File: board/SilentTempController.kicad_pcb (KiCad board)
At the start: 2 copper layers, 100 x 100 mm, 97 parts, among them J1 Barrel_Jack_Switch, J10 Conn_01x02_Pin, J11 Conn_01x02_Pin, J12 Screw_Terminal_01x02, J13 Screw_Terminal_01x02, J14 Screw_Terminal_01x02, J15 Screw_Terminal_01x02, J2 Screw_Terminal_01x02, J3 Conn_01x02_Pin, J4 Screw_Terminal_01x02, J5 Conn_01x02_Pin, J6 Screw_Terminal_01x02, J7 Conn_01x02_Pin, J8 Screw_Terminal_01x02, J9 Conn_01x02_Pin, Q1 2N3904, Q10 2N3904, Q11 2N3906, Q12 IRLZ44N, Q13 2N3904, Q14 2N3904, Q15 2N3906, Q16 IRLZ44N, Q17 2N3904, Q2 2N3906, Q3 IRLZ44N, Q4 2N3904, Q5 2N3904, Q6 2N3904, Q7 2N3906, Q8 IRLZ44N, Q9 2N3904, SW1 SW_Push, SW2 SW_Push, SW3 SW_Push, SW4 SW_Push, SW5 SW_Push, U1 LM7805_TO220

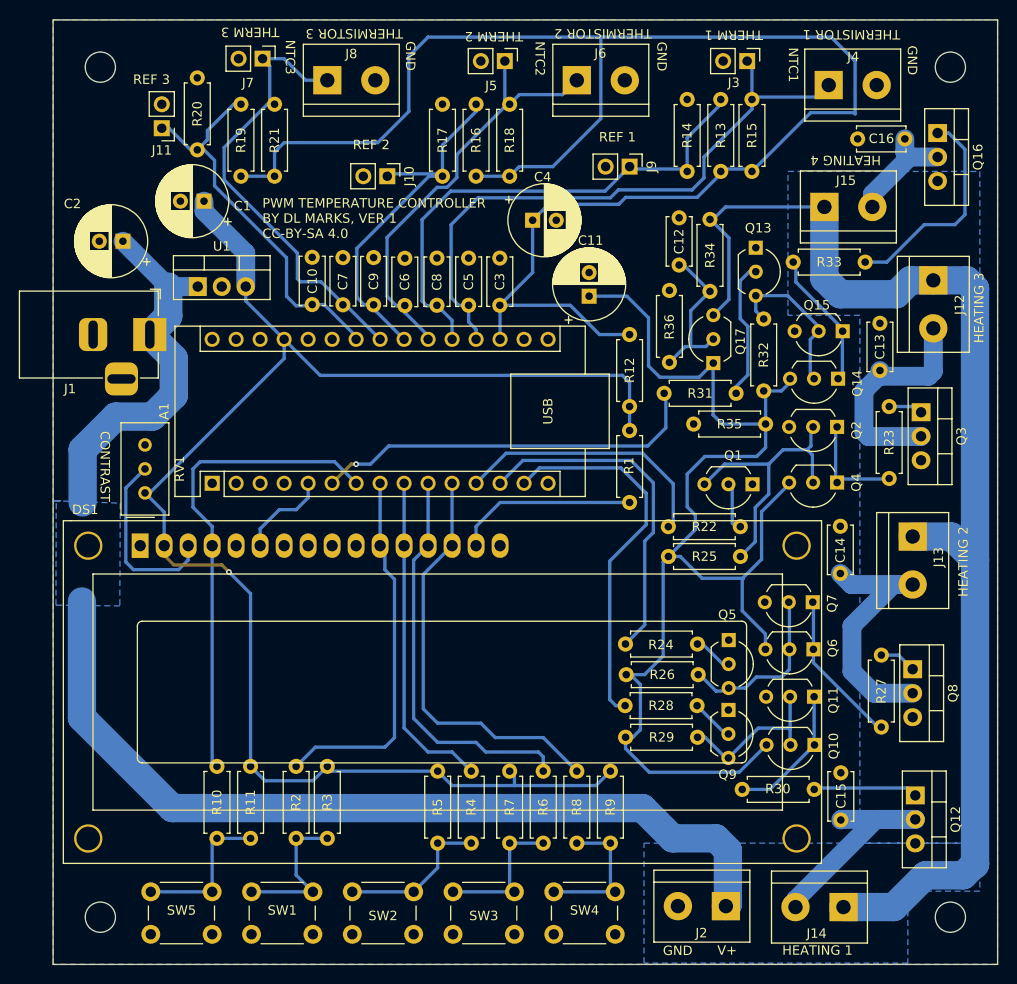
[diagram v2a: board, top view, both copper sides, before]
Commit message: improved snubbers
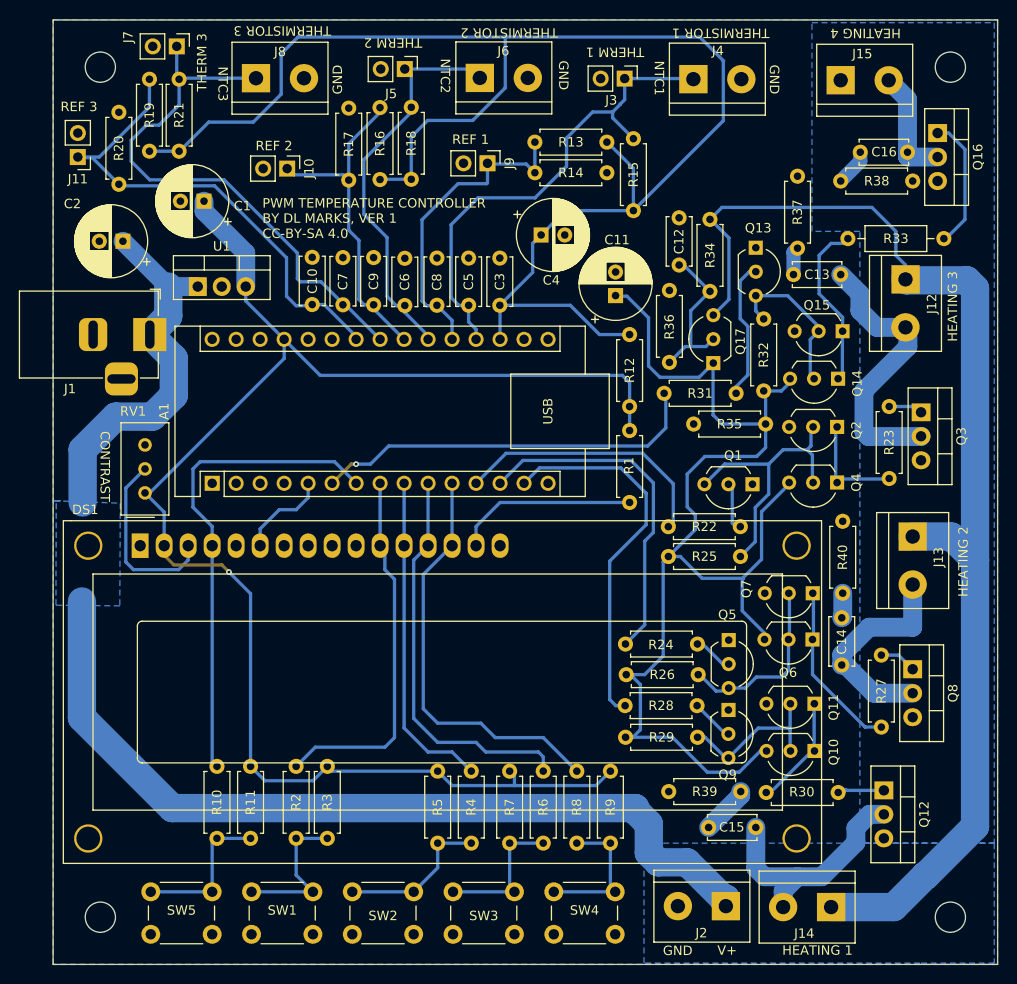
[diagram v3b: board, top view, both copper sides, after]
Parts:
- added R37: 10R, Resistor_THT:R_Axial_DIN0207_L6.3mm_D2.5mm_P7.62mm_Horizontal, F.Cu at (178.8, 66.5)
- added R38: 10R, Resistor_THT:R_Axial_DIN0207_L6.3mm_D2.5mm_P7.62mm_Horizontal, F.Cu at (191.0, 67.1)
- added R39: 10R, Resistor_THT:R_Axial_DIN0207_L6.3mm_D2.5mm_P7.62mm_Horizontal, F.Cu at (165.2, 131.7)
- added R40: 10R, Resistor_THT:R_Axial_DIN0207_L6.3mm_D2.5mm_P7.62mm_Horizontal, F.Cu at (183.6, 103.1)
- C13, C14, C15, C16: value 1000 nF -> 100 nF
- R33: footprint Resistor_THT:R_Axial_DIN0207_L6.3mm_D2.5mm_P7.62mm_Horizontal -> Resistor_THT:R_Axial_DIN0207_L6.3mm_D2.5mm_P10.16mm_Horizontal
- moved R14 16.1 mm to (151.0, 66.2), turned to 0 degrees
- moved J9 15.1 mm to (146.0, 65.2)
- moved J4 14.3 mm to (167.8, 56.3)
- moved J15 13.5 mm to (183.4, 56.4)
- moved R15 13.2 mm to (161.4, 70.2)
- moved J3 13.1 mm to (160.5, 56.2)
- moved R13 12.5 mm to (158.6, 62.9), turned to 180 degrees
- moved C13 11.0 mm to (183.4, 77.0), turned to 180 degrees
- moved J10 10.6 mm to (124.8, 65.7)
- moved J5 10.6 mm to (137.2, 55.2)
- moved R21 10.4 mm to (113.3, 63.9)
- moved R18 10.4 mm to (137.9, 66.9)
- moved J6 10.3 mm to (145.2, 56.1)
- moved R16 10.2 mm to (134.6, 66.9)
- moved R19 10.0 mm to (110.2, 63.9)
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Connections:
- C13 pad 2: GND -> Net-(C13-Pad2)
- C14 pad 2: GND -> Net-(C14-Pad2)
- C15 pad 2: GND -> Net-(C15-Pad2)
- C16 pad 2: GND -> Net-(C16-Pad2)
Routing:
- net /NTC1REF: track 54.4 -> 34.0 mm
- net /VREF: track 175.4 -> 161.6 mm
- net /NTC1: track 66.1 -> 52.7 mm
- net /NTC3REF: track 41.3 -> 52.8 mm
- net /NTC3: track 49.0 -> 59.2 mm
- net Net-(Q16-G): track 23.2 -> 14.1 mm
- net Net-(Q12-G): track 11.1 -> 4.11 mm
- net +24V: track 267.7 -> 261.9 mm
- net Net-(J12-Pin_2): track 24.1 -> 29.6 mm
- net Net-(J13-Pin_2): track 28.6 -> 23.1 mm
- net Net-(C15-Pad2): track 0.00 -> 5.21 mm
- net +12V: track 133.4 -> 128.6 mm
- net Net-(C16-Pad2): track 0.00 -> 3.91 mm
- net /NTC2REF: track 39.7 -> 35.9 mm
- net Net-(Q10-E): track 14.7 -> 11.0 mm
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
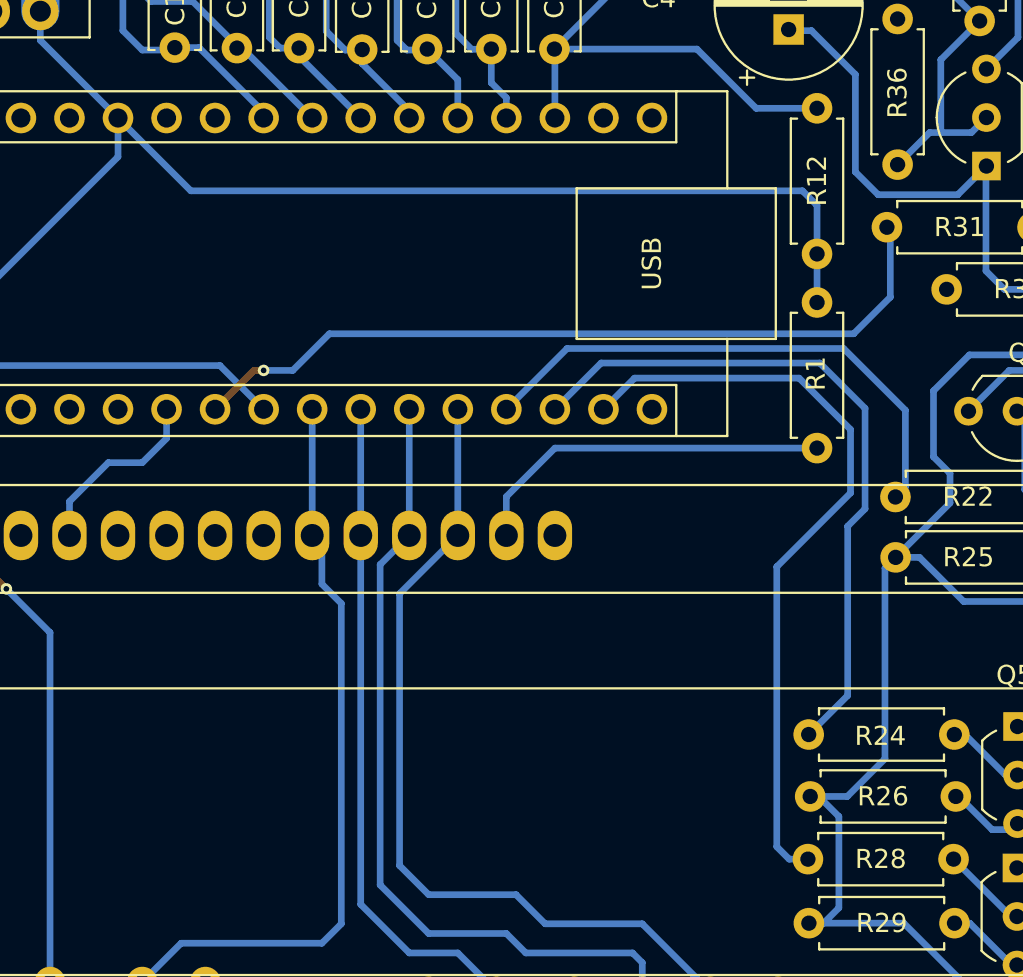
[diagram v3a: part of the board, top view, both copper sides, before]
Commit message: Added on protection
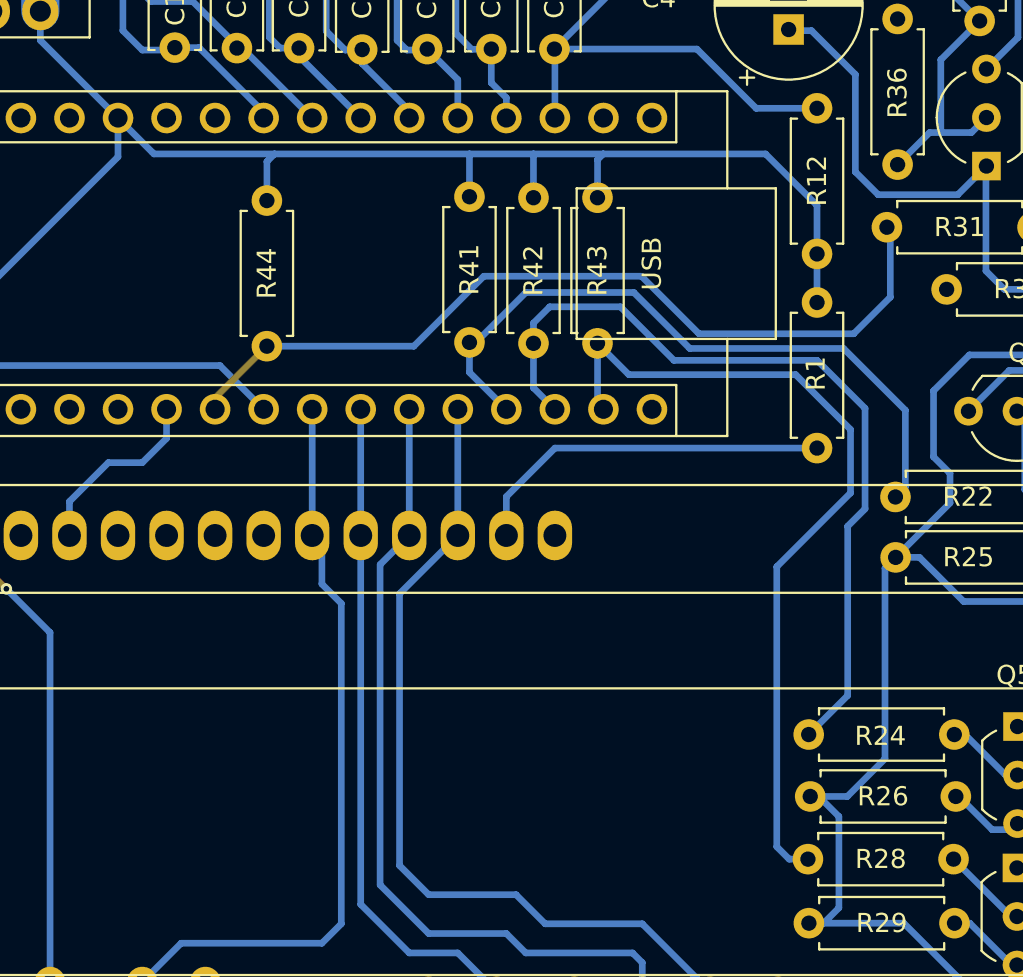
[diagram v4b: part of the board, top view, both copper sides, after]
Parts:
- added R41: 10k, Resistor_THT:R_Axial_DIN0207_L6.3mm_D2.5mm_P7.62mm_Horizontal, F.Cu at (142.8, 87.9)
- added R42: 10k, Resistor_THT:R_Axial_DIN0207_L6.3mm_D2.5mm_P7.62mm_Horizontal, F.Cu at (146.2, 88.0)
- added R43: 10k, Resistor_THT:R_Axial_DIN0207_L6.3mm_D2.5mm_P7.62mm_Horizontal, F.Cu at (149.6, 88.0)
- added R44: 10k, Resistor_THT:R_Axial_DIN0207_L6.3mm_D2.5mm_P7.62mm_Horizontal, F.Cu at (132.2, 88.1)
- R25, R26, R29, R32, R35: value 2k2 -> 4k7
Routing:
- net +5V: track 163.5 -> 173.0 mm
- net /OC1A: track 28.3 -> 35.5 mm
- net /OC1B: track 36.5 -> 43.2 mm
- net /OC2A: track 40.0 -> 44.0 mm
- net /OC2B: track 41.5 -> 44.3 mm, vias 1 -> 0

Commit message: JLCPCB order
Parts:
- moved R22 3.11 mm to (171.1, 106.2)
- moved R43 3.10 mm to (146.4, 88.0)
- moved R25 3.10 mm to (163.4, 109.4)
- moved R42 2.95 mm to (143.2, 88.0)
- moved R41 2.85 mm to (140.0, 88.0)
- moved Q9 2.41 mm to (171.6, 120.7)
- moved Q5 2.26 mm to (171.6, 113.4)
- moved Q6 0.63 mm to (180.6, 116.2)
- moved Q7 0.48 mm to (180.6, 111.2)
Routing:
- net /OC1A: track 35.5 -> 44.8 mm
- net /OC1B: track 43.2 -> 48.2 mm
- net /OC2A: track 44.0 -> 48.3 mm
- net Net-(Q1-C): track 29.8 -> 33.2 mm
- net Net-(Q1-B): track 5.29 -> 7.61 mm
- net Net-(Q10-B): track 17.1 -> 15.3 mm
- net /NTC1REF: track 34.0 -> 32.2 mm
- net Net-(Q5-C): track 19.4 -> 17.9 mm
- net +12V: track 128.6 -> 129.5 mm
- net Net-(Q9-B): track 4.56 -> 3.66 mm
- net /VREF: track 161.6 -> 160.7 mm
- net Net-(Q5-B): track 4.19 -> 3.44 mm
